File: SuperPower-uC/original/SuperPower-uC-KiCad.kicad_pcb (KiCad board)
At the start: 2 copper layers, 90 x 90 mm, 164 parts, among them J1 JST_PH_S2B_thru, J2 Barrel_Jack_Switch, J3 DNP/Screw_Terminal_01x02, J4 DNP/JST_ZH_S2B_thru, J5 JST_XH_S2B_thru, J6 Conn_01x02_Male, J7 mcu_pinout, J8 mcu_pinout, Q1 DMN2019UTS, Q10 2N7002A, Q11 2N7002A, Q2 DMP3028LSD, Q3 DMN3018SSD, Q4 2N7002A, Q5 DMP3028LSD, Q6 2N7002A, Q7 S8050, Q8 S8050, Q9 DMN3018SSD, SW1 DNP/SKRKAEE020, U1 AP9101CK6-AYTRG1, U10 TPS63070RNMT, U2 USB-C, U3 IP4220CZ6, U4 LTC4162EUFD-LAD, U5 RV-3028-C7, U6 CP2102N-A01-GQFN28, U7 ESP32-WROOM32, U8 TPS70933DRVT, U9 TPS63070RNMT

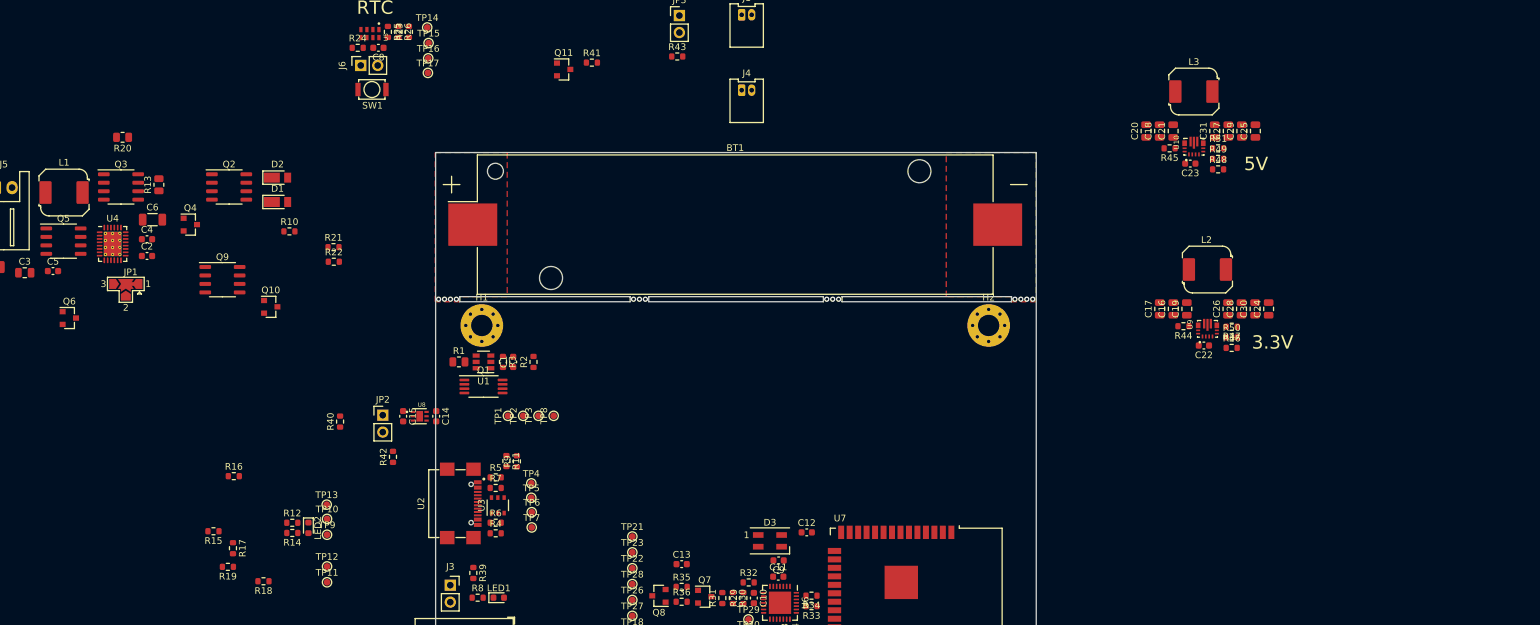
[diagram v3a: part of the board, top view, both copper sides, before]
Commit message: Replace some dual P-MOSFETs by SOT23-6 P-MOSFETs
+ resolve some issues (2 P-MOSFETs at Buck-Boost stage were reversed)
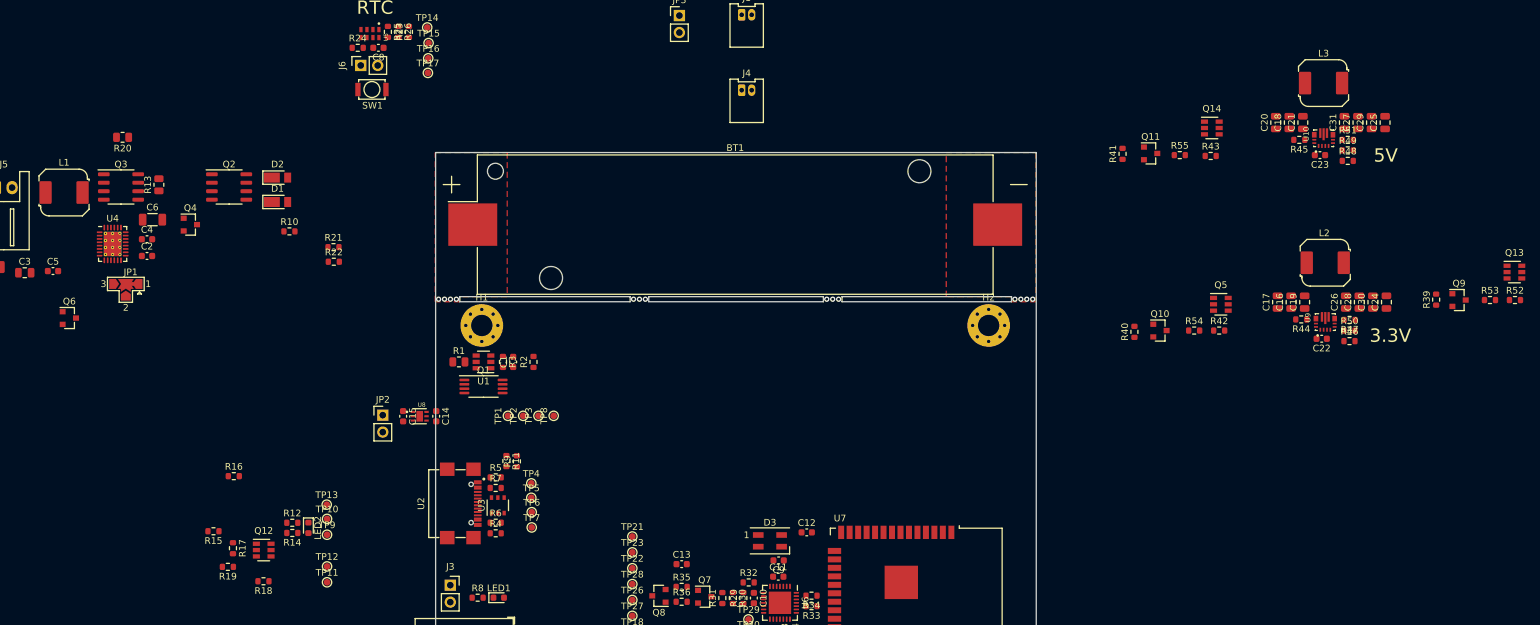
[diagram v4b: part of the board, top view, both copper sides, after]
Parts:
- added Q12: DMP2035UVT, Package_TO_SOT_SMD:SOT-23-6, F.Cu at (89.2, 99.6)
- added Q13: DMP2035UVT, Package_TO_SOT_SMD:SOT-23-6, F.Cu at (276.6, 57.9)
- added Q14: DMP2035UVT, Package_TO_SOT_SMD:SOT-23-6, F.Cu at (231.3, 36.3)
- added R52: 1M, Resistor_SMD:R_0603_1608Metric, F.Cu at (276.7, 62.1)
- added R53: 390k, Resistor_SMD:R_0603_1608Metric, F.Cu at (273.0, 62.1)
- added R54: 390k, Resistor_SMD:R_0603_1608Metric, F.Cu at (228.7, 66.7)
- added R55: 390k, Resistor_SMD:R_0603_1608Metric, F.Cu at (226.5, 40.4)
- Q5: value DMP3028LSD -> DMP2035UVT; footprint Package_SO:SO-8_3.9x4.9mm_P1.27mm -> Package_TO_SOT_SMD:SOT-23-6
- Q9: value DMN3018SSD -> 2N7002A; footprint Package_SO:SO-8_3.9x4.9mm_P1.27mm -> Package_TO_SOT_SMD:SOT-23
- R39: value 100k -> 1M
- moved Q9 185.3 mm to (268.4, 62.1)
- moved Q5 173.7 mm to (232.7, 62.7)
- moved R39 150.0 mm to (264.9, 62.0), turned to 90 degrees
- moved Q10 133.3 mm to (223.5, 66.7)
- moved R42 125.2 mm to (232.4, 66.7), turned to 0 degrees
- moved R40 119.8 mm to (219.7, 66.9)
- moved Q11 88.8 mm to (222.1, 40.1)
- moved R43 81.3 mm to (231.1, 40.5)
- moved R41 80.7 mm to (217.9, 40.2), turned to 90 degrees
- moved C20 19.5 mm to (240.9, 35.5)
- moved C21 19.5 mm to (244.9, 35.5)
- moved C25 19.5 mm to (257.3, 35.5)
- moved C27 19.5 mm to (253.2, 35.5)
- moved C29 19.5 mm to (255.2, 35.5)
- moved L3 19.5 mm to (248.1, 29.6)
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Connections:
- Q5 pad 1: VCC -> Net-(C16-Pad1)
- Q5 pad 2: Net-(Q5-Pad2) -> Net-(C16-Pad1)
- Q5 pad 3: Net-(C16-Pad1) -> Net-(Q5-Pad3)
- Q5 pad 4: Net-(JP2-Pad1) -> /Regulator and Cut-Off Module/VIN
- Q5 pad 5: /Regulator and Cut-Off Module/VIN -> Net-(C16-Pad1)
- Q5 pad 6: /Regulator and Cut-Off Module/VIN -> Net-(C16-Pad1)
- Q9 pad 1: GND -> /MCU Module/EN_3V3
- Q9 pad 2: /MCU Module/EN_3V3 -> GND
- Q9 pad 3: Net-(C18-Pad1) -> Net-(Q9-Pad3)
- R17 pad 2: Net-(Q5-Pad2) -> Net-(Q12-Pad3)
- R19 pad 1: Net-(Q5-Pad2) -> Net-(Q12-Pad3)
- R42 pad 1: Net-(JP2-Pad1) -> Net-(Q5-Pad3)
- R43 pad 1: Net-(JP3-Pad1) -> Net-(Q14-Pad3)

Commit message: Moved some parts around
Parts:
- moved JP2 128.8 mm to (235.3, 67.7), turned to 90 degrees
- moved J4 114.8 mm to (47.0, 36.7), turned to 270 degrees
- moved JP3 86.3 mm to (235.1, 40.9), turned to 90 degrees
- moved J1 69.5 mm to (119.8, 74.8), turned to 270 degrees
- moved R18 63.8 mm to (63.6, 45.8)
- moved Q6 63.6 mm to (110.1, 25.5)
- moved C14 63.5 mm to (65.3, 40.0)
- moved C15 63.5 mm to (60.4, 40.0)
- moved U8 63.5 mm to (62.8, 40.0)
- moved Q12 48.7 mm to (53.5, 66.5)
- moved R19 48.4 mm to (50.7, 66.9), turned to 90 degrees
- moved R12 47.9 mm to (59.3, 62.0)
- moved R14 47.7 mm to (59.2, 63.9)
- moved LED2 45.8 mm to (70.9, 57.9), turned to 180 degrees
- moved R21 45.0 mm to (57.0, 40.0), turned to 90 degrees
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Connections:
- J1 pad 1: -BATT -> +BATT
- J1 pad 2: +BATT -> -BATT
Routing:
- added copper zone on F.Cu, net GND

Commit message: Add 3D file to every component
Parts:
- D3: footprint LED_SMD:LED_SK6812MINI_PLCC4_3.5x3.5mm_P1.75mm -> LED_SMD:LED_SK6812_PLCC4_5.0x5.0mm_P3.2mm
- J2: footprint Connector_BarrelJack:BarrelJack_Horizontal -> Connector_BarrelJack:BarrelJack_CUI_PJ-102AH_Horizontal
- JP2, JP3: footprint Connector_PinHeader_2.54mm:PinHeader_1x02_P2.54mm_Vertical -> Jumper:SolderJumper-2_P1.3mm_Open_TrianglePad1.0x1.5mm
- moved R21 108.7 mm to (153.2, 90.8)
- moved U8 108.7 mm to (159.0, 90.8)
- moved C14 108.7 mm to (161.4, 90.8)
- moved C15 108.7 mm to (156.5, 90.8)
- moved R22 108.7 mm to (154.8, 90.8)
- moved Q13 105.9 mm to (174.3, 115.6)
- moved Q9 105.9 mm to (166.0, 119.8)
- moved R52 105.9 mm to (174.4, 119.8)
- moved R39 105.9 mm to (163.3, 119.8)
- moved R53 105.9 mm to (170.6, 119.8)
- moved R15 103.1 mm to (154.8, 80.0)
- moved R14 99.9 mm to (157.9, 80.0)
- moved R12 99.9 mm to (157.9, 78.5)
- moved R16 99.8 mm to (154.8, 78.5), turned to 0 degrees
- moved C8 99.2 mm to (133.1, 119.8)
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
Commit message: PLaced BATT+ and - solid tracks
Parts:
- moved L3 0.58 mm to (184.9, 67.1)
- moved Q1 0.54 mm to (125.9, 75.2)
- moved C1 0.51 mm to (129.9, 71.6)
- moved R2 0.51 mm to (133.0, 71.6)
- moved R3 0.51 mm to (128.4, 71.6)
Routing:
- net -BATT: vias 4 -> 3
- net (no net): vias 6 -> 7
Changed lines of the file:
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@@
   )
   (module SPM6530T-1R5M:L_TDK_SPM6530T (layer F.Cu)
-    (at 185.185 66.548 180)
+    (at 184.912 67.056 180)
     (descr "Inductor, TDK, SPM6530T, 7.1x6.5x3.0mm (https://product.tdk.com/info/en/catalog/datasheets/inductor_commercial_power_spm6530_en.pdf)")
     (tags "Inductor TDK_SPM6530T")
@@
   )
   (module Resistor_SMD:R_0603_1608Metric (layer F.Cu)
-    (at 132.969 71.12 90)
+    (at 132.969 71.628 90)
     (descr "Resistor SMD 0603 (1608 Metric), square (rectangular) end terminal, IPC_7351 nominal, (Body size source: IPC-SM-782 page 72, https://www.pcb-3d.com/wordpress/wp-content/uploads/ipc-sm-782a_amendment_1_and_2.pdf), generated with kicad-footprint-generator")
     (tags resistor)
@@
   )
   (module Resistor_SMD:R_0603_1608Metric (layer F.Cu)
-    (at 128.397 71.12 270)
+    (at 128.397 71.628 270)
     (descr "Resistor SMD 0603 (1608 Metric), square (rectangular) end terminal, IPC_7351 nominal, (Body size source: IPC-SM-782 page 72, https://www.pcb-3d.com/wordpress/wp-content/uploads/ipc-sm-782a_amendment_1_and_2.pdf), generated with kicad-footprint-generator")
     (tags resistor)
@@
   )
   (module Package_SO:TSSOP-8_4.4x3mm_P0.65mm (layer F.Cu)
-    (at 125.476 74.803)
+    (at 125.857 75.184)
     (descr "TSSOP, 8 Pin (JEDEC MO-153 Var AA https://www.jedec.org/document_search?search_api_views_fulltext=MO-153), generated with kicad-footprint-generator ipc_gullwing_generator.py")
     (tags "TSSOP SO")
@@
   )
   (module Capacitor_SMD:C_0603_1608Metric (layer F.Cu)
-    (at 129.921 71.12 90)
+    (at 129.921 71.628 90)
     (descr "Capacitor SMD 0603 (1608 Metric), square (rectangular) end terminal, IPC_7351 nominal, (Body size source: IPC-SM-782 page 76, https://www.pcb-3d.com/wordpress/wp-content/uploads/ipc-sm-782a_amendment_1_and_2.pdf), generated with kicad-footprint-generator")
     (tags capacitor)
@@
   (via (at 174.498 61.976) (size 0.8) (drill 0.4) (layers F.Cu B.Cu) (net 0))
   (via (at 173.609 61.976) (size 0.8) (drill 0.4) (layers F.Cu B.Cu) (net 0))
-  (via (at 146.431 61.976) (size 0.8) (drill 0.4) (layers F.Cu B.Cu) (net 0))
-  (via (at 145.542 61.976) (size 0.8) (drill 0.4) (layers F.Cu B.Cu) (net 0))
-  (via (at 144.653 61.976) (size 0.8) (drill 0.4) (layers F.Cu B.Cu) (net 0))
-  (via (at 201.803 61.976) (size 0.8) (drill 0.4) (layers F.Cu B.Cu) (net 1))
-  (via (at 202.692 61.976) (size 0.8) (drill 0.4) (layers F.Cu B.Cu) (net 1))
-  (via (at 203.581 61.976) (size 0.8) (drill 0.4) (layers F.Cu B.Cu) (net 1))
-  (via (at 204.47 61.976) (size 0.8) (drill 0.4) (layers F.Cu B.Cu) (net 1))
+  (via (at 146.431 61.976) (size 0.8) (drill 0.4) (layers F.Cu B.Cu) (net 1))
+  (via (at 145.542 61.976) (size 0.8) (drill 0.4) (layers F.Cu B.Cu) (net 1))
+  (via (at 144.653 61.976) (size 0.8) (drill 0.4) (layers F.Cu B.Cu) (net 1))
+  (via (at 201.803 61.976) (size 0.8) (drill 0.4) (layers F.Cu B.Cu) (net 0))
+  (via (at 202.692 61.976) (size 0.8) (drill 0.4) (layers F.Cu B.Cu) (net 0))
+  (via (at 203.581 61.976) (size 0.8) (drill 0.4) (layers F.Cu B.Cu) (net 0))
+  (via (at 204.47 61.976) (size 0.8) (drill 0.4) (layers F.Cu B.Cu) (net 0))
   (via (at 115.443 61.976) (size 0.8) (drill 0.4) (layers F.Cu B.Cu) (net 2))
   (via (at 116.332 61.976) (size 0.8) (drill 0.4) (layers F.Cu B.Cu) (net 2))
@@
     )
   )
+  (zone (net 4) (net_name GND) (layer F.Cu) (hatch edge 0.508)
+    (connect_pads (clearance 0.508))
+    (min_thickness 0.254)
+    (fill yes (arc_segments 32) (thermal_gap 0.508) (thermal_bridge_width 0.508))
+    (polygon
+      (pts
+        (xy 228.6 143.383) (xy 93.599 140.97) (xy 102.997 30.861) (xy 215.646 30.607)
+      )
+    )
+  )
   (zone (net 1) (net_name -BATT) (layer F.Cu) (hatch edge 0.508)
     (connect_pads (clearance 0.508))
@@
     (polygon
       (pts
-        (xy 204.978 62.357) (xy 201.295 62.357) (xy 201.295 61.595) (xy 191.516 61.595) (xy 191.516 40.005)
-        (xy 204.978 40.005)
+        (xy 203.454 54.356) (xy 146.939 54.356) (xy 146.939 62.357) (xy 144.145 62.357) (xy 144.145 47.117)
+        (xy 203.454 47.117)
       )
     )
   )
-  (zone (net 4) (net_name GND) (layer F.Cu) (hatch edge 0.508)
+  (zone (net 1) (net_name -BATT) (layer F.Cu) (hatch edge 0.508)
+    (connect_pads (clearance 0.508))
+    (min_thickness 0.254)
+    (fill yes (arc_segments 32) (thermal_gap 0.508) (thermal_bridge_width 0.508))
+    (polygon
+      (pts
+        (xy 146.939 69.215) (xy 138.938 69.215) (xy 138.938 71.501) (xy 129.159 71.501) (xy 129.286 62.357)
+        (xy 146.939 62.357)
+      )
+    )
+  )
+  (zone (net 2) (net_name +BATT) (layer F.Cu) (hatch edge 0.508)
     (connect_pads (clearance 0.508))
     (min_thickness 0.254)
@@
     (polygon
       (pts
-        (xy 282.321 14.605) (xy 281.178 163.576) (xy 24.257 162.687) (xy 22.098 13.208)
+        (xy 118.618 70.104) (xy 121.666 70.104) (xy 121.666 73.406) (xy 121.031 73.406) (xy 121.031 74.803)
+        (xy 115.062 74.803) (xy 115.062 62.357) (xy 118.618 62.357)
       )
     )

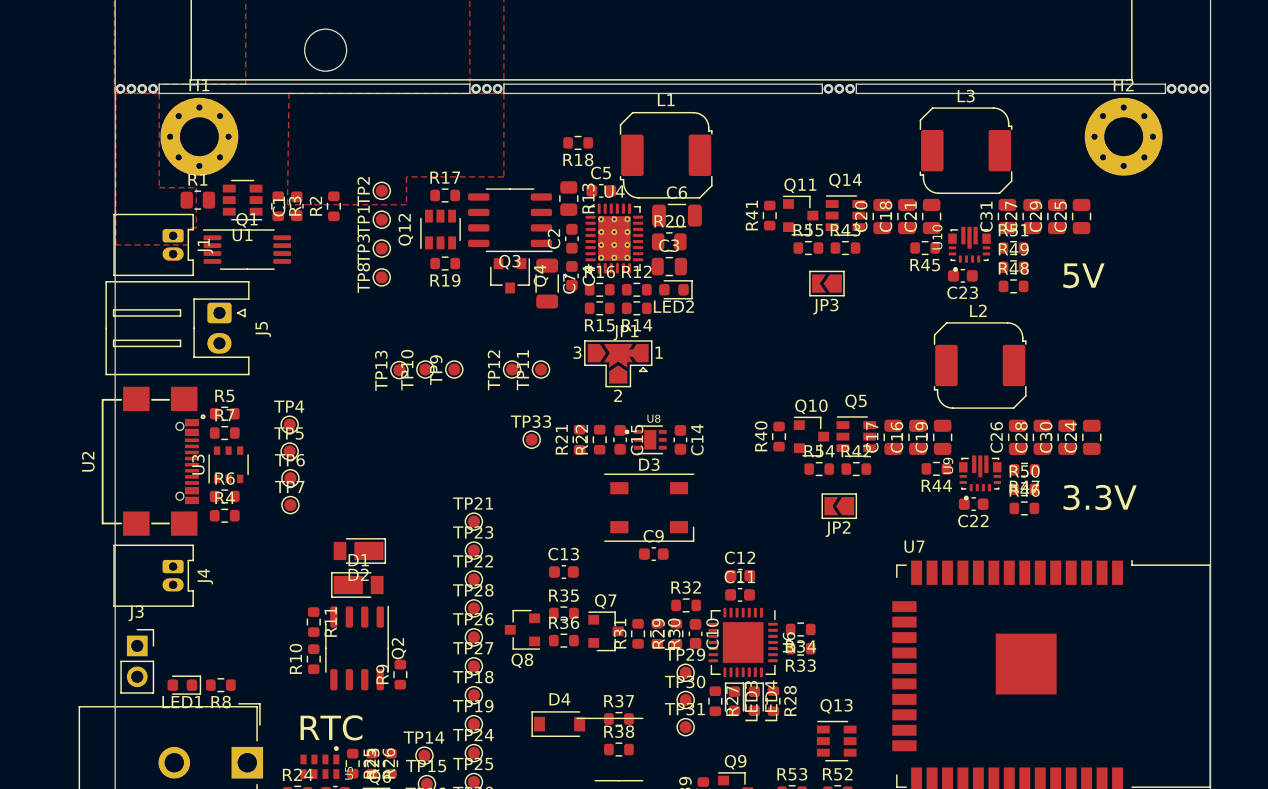
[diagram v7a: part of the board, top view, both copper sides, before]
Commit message: Remove R40 + Update Terminal Block Footprint
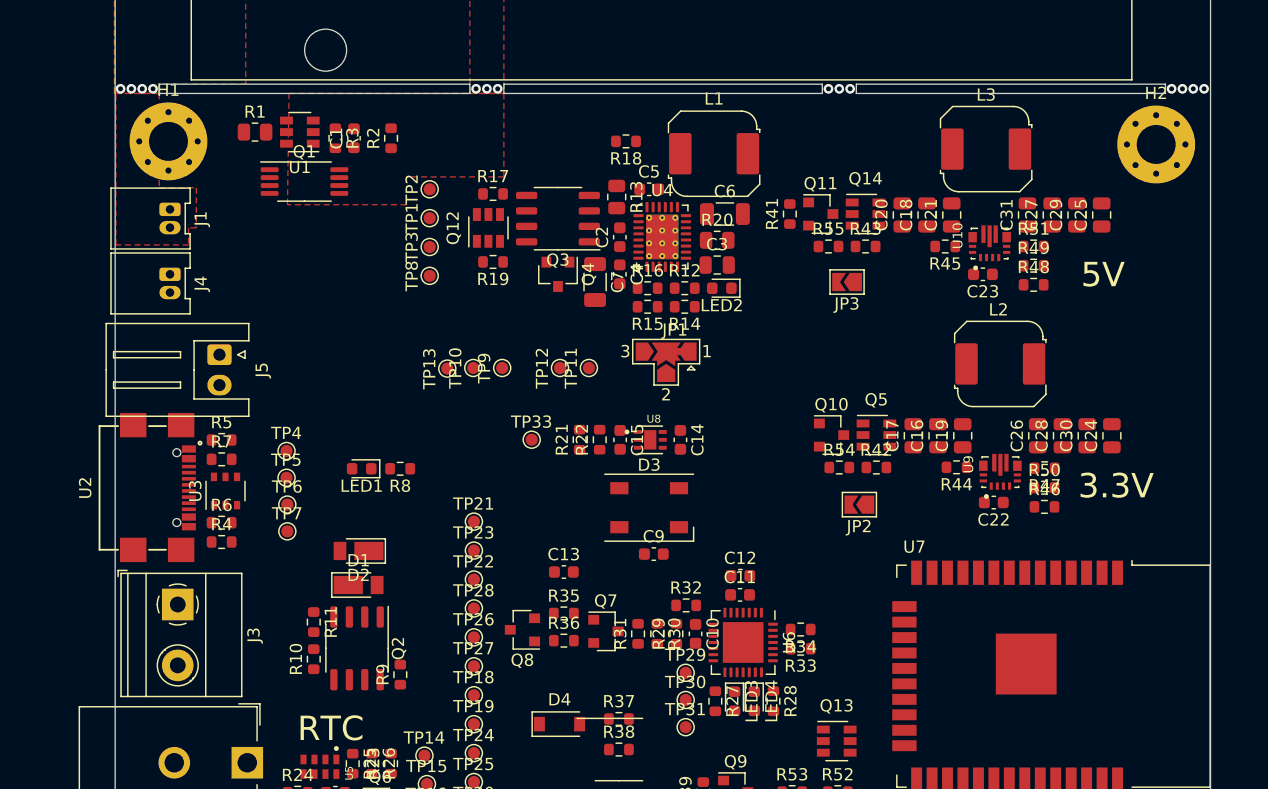
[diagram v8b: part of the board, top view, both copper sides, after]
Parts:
- removed R40: 1M, Resistor_SMD:R_0603_1608Metric
- J3: footprint Connector_PinSocket_2.54mm:PinSocket_1x02_P2.54mm_Vertical -> TerminalBlock_Phoenix:TerminalBlock_Phoenix_MKDS-1,5-2_1x02_P5.00mm_Horizontal
- moved J4 24.0 mm to (119.5, 78.0)
- moved LED1 23.1 mm to (135.3, 93.2)
- moved R8 23.1 mm to (138.4, 93.2)
- moved U1 7.30 mm to (130.2, 65.5)
- moved R1 7.30 mm to (126.5, 65.5)
- moved C1 7.30 mm to (134.6, 66.0)
- moved Q1 7.30 mm to (130.6, 69.6)
- moved R2 7.30 mm to (137.7, 66.0)
- moved R3 7.30 mm to (133.1, 66.0)
- moved J3 4.76 mm to (120.1, 104.3), turned to 270 degrees
- moved C3 3.94 mm to (164.5, 76.5)
- moved C4 3.94 mm to (156.5, 77.2)
- moved C5 3.94 mm to (158.9, 70.2)
- moved LED2 3.94 mm to (164.8, 78.4)
- moved R12 3.94 mm to (161.8, 78.4)
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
